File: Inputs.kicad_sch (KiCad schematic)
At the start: 1 part, among them J4 Conn_01x04

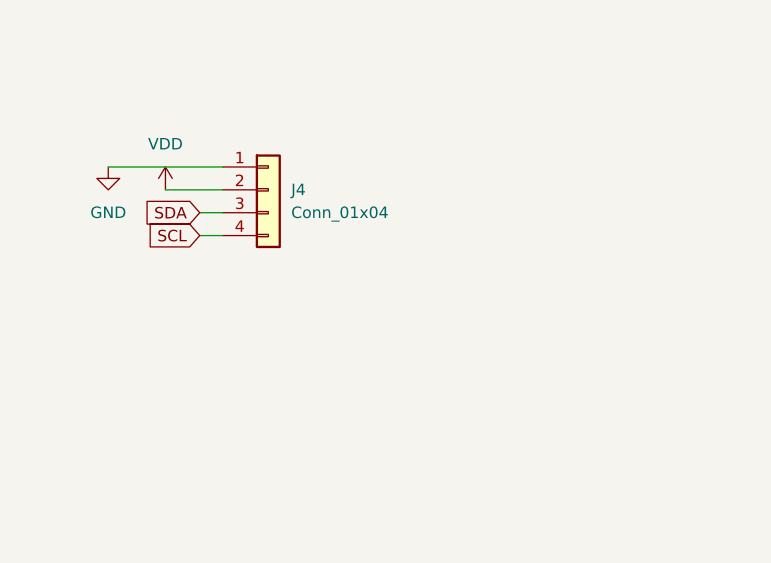
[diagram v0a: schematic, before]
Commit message: Added microphone, fuse
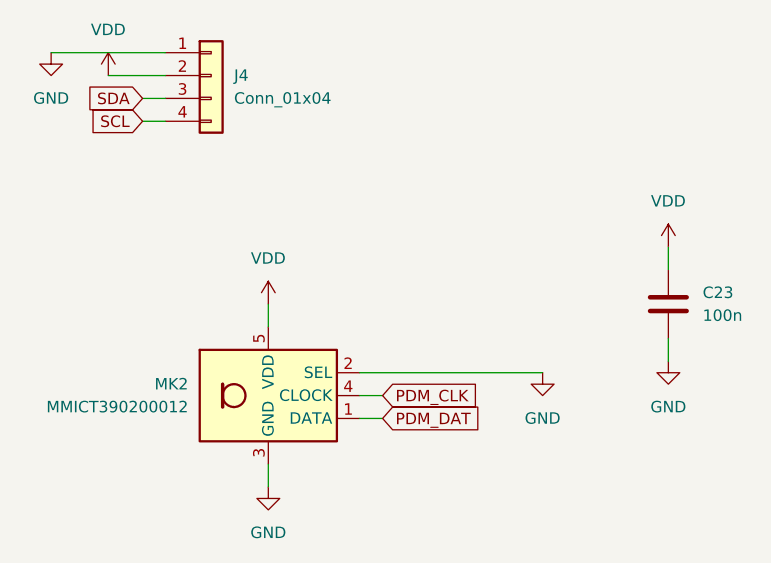
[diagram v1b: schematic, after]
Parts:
- added C23: 100n, symbol Device:C
- added MK2: MMICT390200012, Sensor_Audio:Knowles_LGA-5_3.5x2.65mm, symbol Sensor_Audio:SPH0641LU4H-1
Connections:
- net GND: now also C23.2, MK2.2 (SEL), MK2.3 (GND)
- net VDD: now also C23.1, MK2.5 (VDD)
- new net PDM_CLK: MK2.4 (CLOCK)
- new net PDM_DAT: MK2.1 (DATA)
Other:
- moved on the sheet: J4

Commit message: finished schematic
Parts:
- C23: value 100n -> .1u; footprint (none) -> Capacitor_SMD:C_0603_1608Metric; LCSC PN (none) -> C14663
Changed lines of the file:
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@@
 			)
 		)
-		(property "Value" "100n"
+		(property "Value" ".1u"
 			(at 101.6 52.0699 0)
 			(effects
@@
 			)
 		)
-		(property "Footprint" ""
+		(property "Footprint" "Capacitor_SMD:C_0603_1608Metric"
 			(at 98.7552 54.61 0)
 			(effects
@@
 			(at 97.79 50.8 0)
 			(effects
+				(font
+					(size 1.27 1.27)
+				)
+				(hide yes)
+			)
+		)
+		(property "LCSC PN" "C14663"
+			(at 97.79 50.8 0)
+			(effects

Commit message: Made modifications from fabrication
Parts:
- C23: MPN (none) -> C14663
- J4: MPN (none) -> C160390
- MK2: MPN (none) -> C3171752
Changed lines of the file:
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@@
+			)
+		)
+		(property "MPN" "C14663"
+			(at 97.79 50.8 0)
+			(effects
+				(font
+					(size 1.27 1.27)
+				)
+				(hide yes)
 			)
 		)
@@
 			)
 		)
+		(property "MPN" "C160390"
+			(at 46.99 25.4 0)
+			(effects
+				(font
+					(size 1.27 1.27)
+				)
+				(hide yes)
+			)
+		)
 		(pin "2"
 		)
@@
 			(at 53.34 60.96 0)
 			(effects
+				(font
+					(size 1.27 1.27)
+				)
+				(hide yes)
+			)
+		)
+		(property "MPN" "C3171752"
+			(at 53.34 60.96 0)
+			(effects
